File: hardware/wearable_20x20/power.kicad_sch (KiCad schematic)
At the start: 27 parts, among them U1 BQ25185, U2 TPS7A2033PDBVR, U3 TPS63802DLAR, U4 TPS22917DBVR, U5 TPS22917DBVR

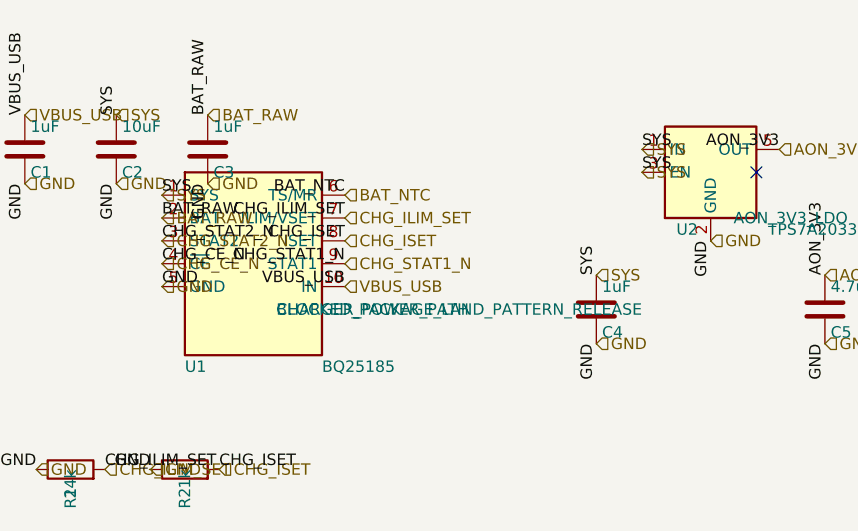
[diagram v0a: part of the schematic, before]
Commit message: Release verified charger and sensor footprints
Co-authored-by: illiapliukhin <illiapliukhin@users.noreply.github.com>
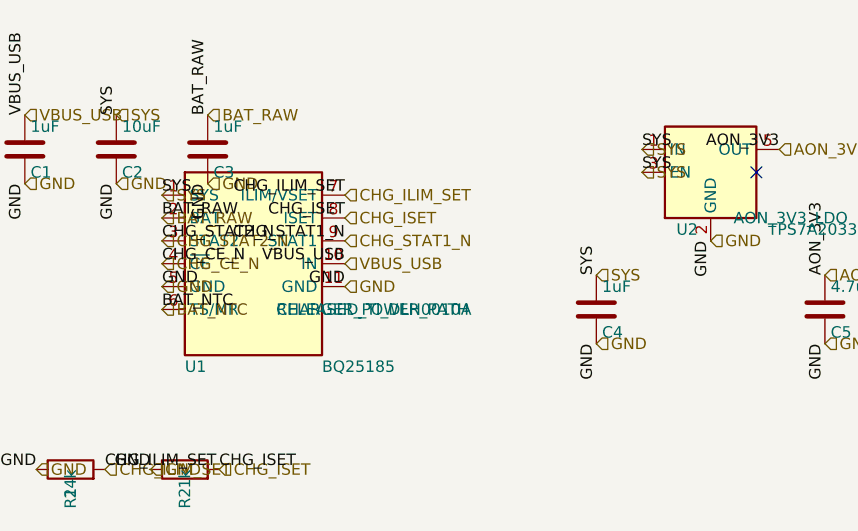
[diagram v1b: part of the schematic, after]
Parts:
- U1: footprint (none) -> Package_DFN_QFN:Texas_DLH0010A_WSON-10-1EP_2.2x2mm_P0.4mm_EP0.9x1.5mm; FootprintStatus BLOCKED_PACKAGE_LAND_PATTERN_RELEASE -> RELEASED_TI_DLH0010A
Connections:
- net GND: now also U1.11 (GND)

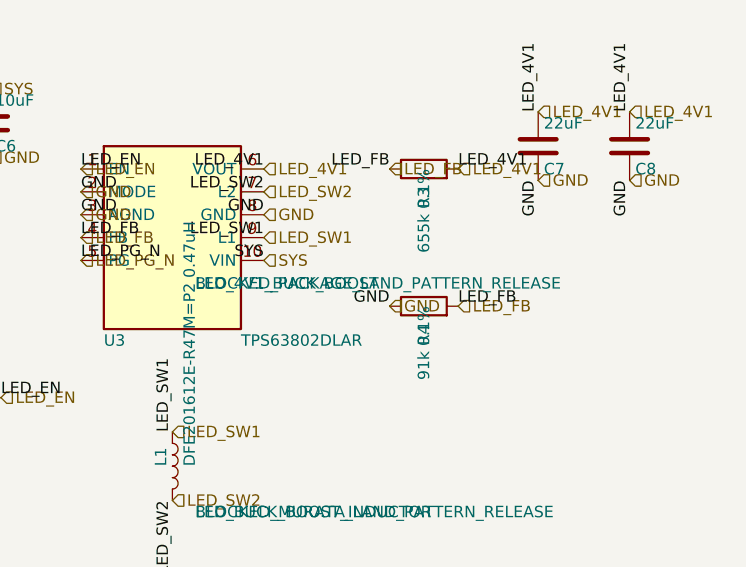
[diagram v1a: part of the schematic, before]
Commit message: Release exact TPS63802 HotRod footprint
Co-authored-by: illiapliukhin <illiapliukhin@users.noreply.github.com>
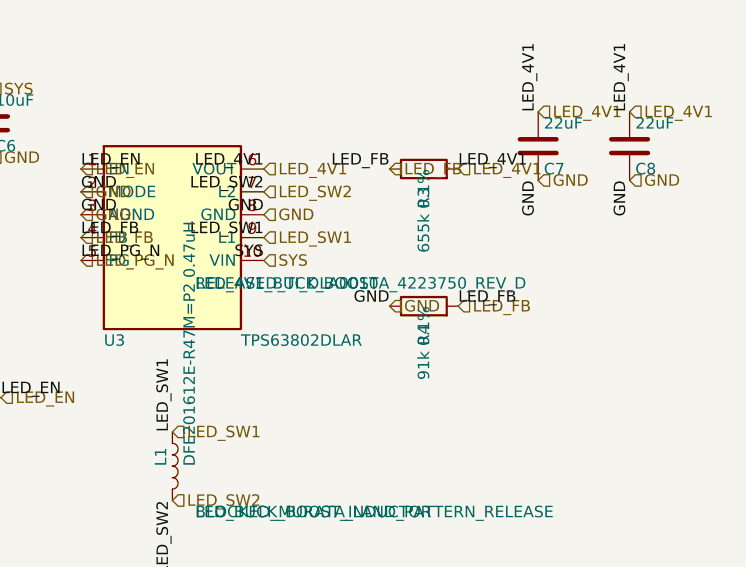
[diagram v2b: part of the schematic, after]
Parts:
- U3: footprint (none) -> PartSignal_Packages:TI_DLA0010A_VSON-HR-10_2x3mm_P0.5mm; FootprintStatus BLOCKED_PACKAGE_LAND_PATTERN_RELEASE -> RELEASED_TI_DLA0010A_4223750_REV_D
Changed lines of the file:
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@@
 			)
 		)
-		(property "Footprint" ""
+		(property "Footprint" "PartSignal_Packages:TI_DLA0010A_VSON-HR-10_2x3mm_P0.5mm"
 			(at 157.48 55.88 0)
 			(hide yes)
@@
 			)
 		)
-		(property "FootprintStatus" "BLOCKED_PACKAGE_LAND_PATTERN_RELEASE"
+		(property "FootprintStatus" "RELEASED_TI_DLA0010A_4223750_REV_D"
 			(at 160.02 60.9599 0)
 			(show_name no)

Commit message: Release crystal and power inductor packages
Co-authored-by: illiapliukhin <illiapliukhin@users.noreply.github.com>
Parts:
- L1: footprint (none) -> PartSignal_Packages:Murata_DFE201612E_2.0x1.6mm; FootprintStatus BLOCKED_MURATA_LAND_PATTERN_RELEASE -> RELEASED_MURATA_DFE201612E
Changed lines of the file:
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@@
 			)
 		)
-		(property "Footprint" ""
+		(property "Footprint" "PartSignal_Packages:Murata_DFE201612E_2.0x1.6mm"
 			(at 157.48 81.28 0)
 			(hide yes)
@@
 			)
 		)
-		(property "FootprintStatus" "BLOCKED_MURATA_LAND_PATTERN_RELEASE"
+		(property "FootprintStatus" "RELEASED_MURATA_DFE201612E"
 			(at 160.02 86.3599 0)
 			(show_name no)
